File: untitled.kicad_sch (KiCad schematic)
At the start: 10 parts, among them IC1 MSPM0C1103SDGS20R, J1 Conn_01x10_Socket, SW1 SW_MEC_5G, SW2 SW_MEC_5G, U1 FZ2812-5050

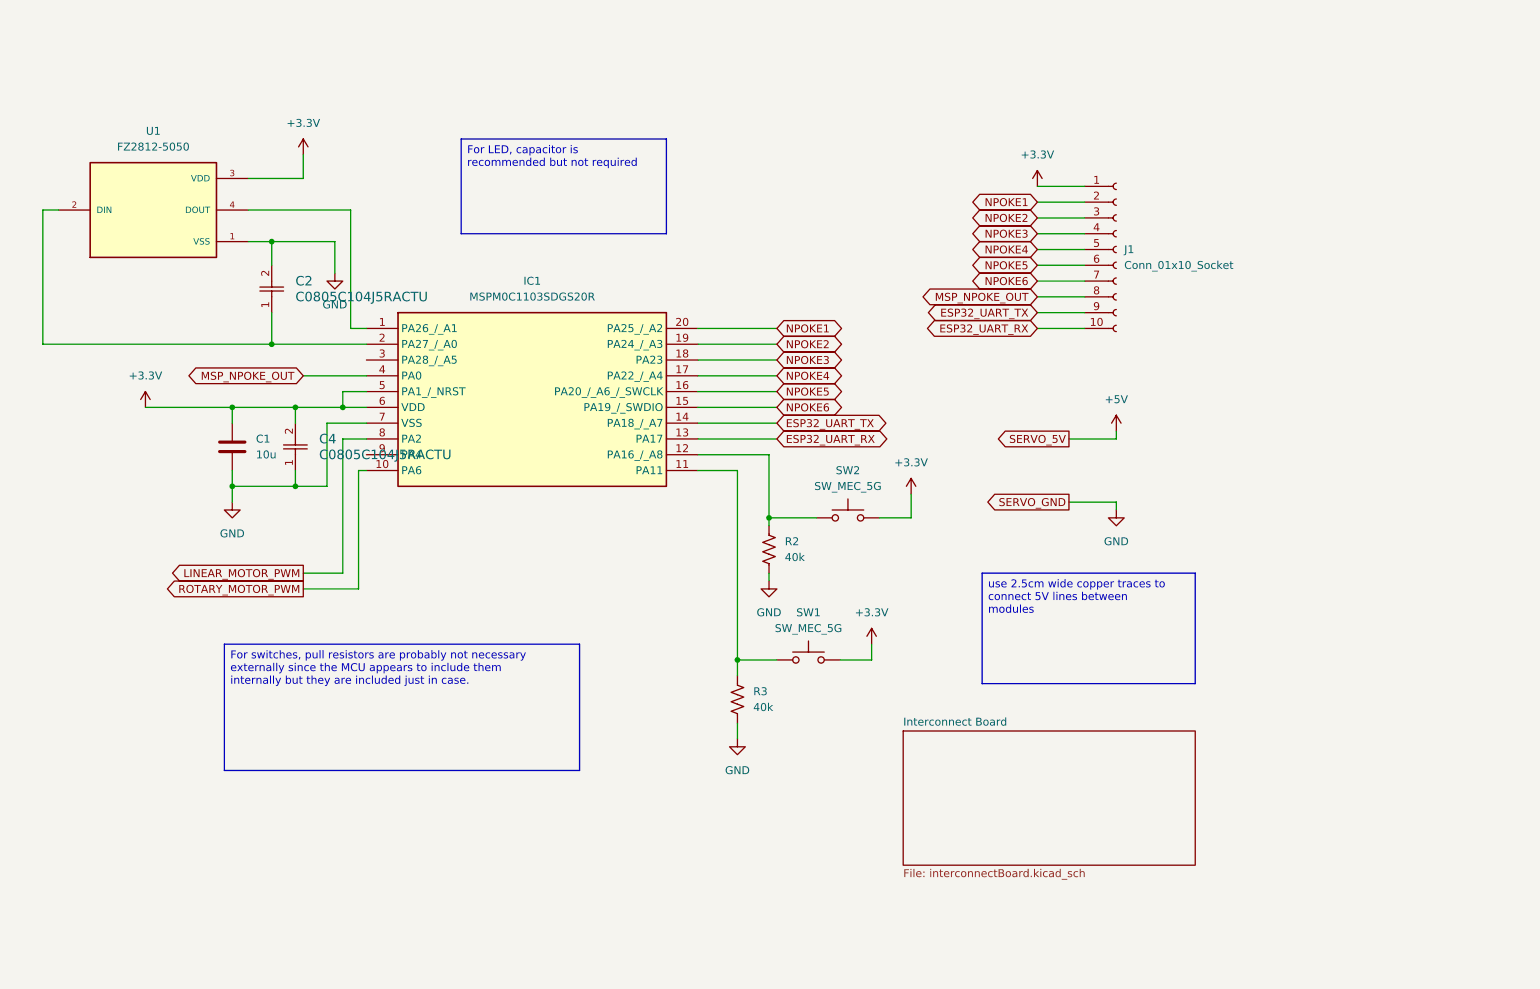
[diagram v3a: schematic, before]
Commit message: schem Rev 1 Ready for layout
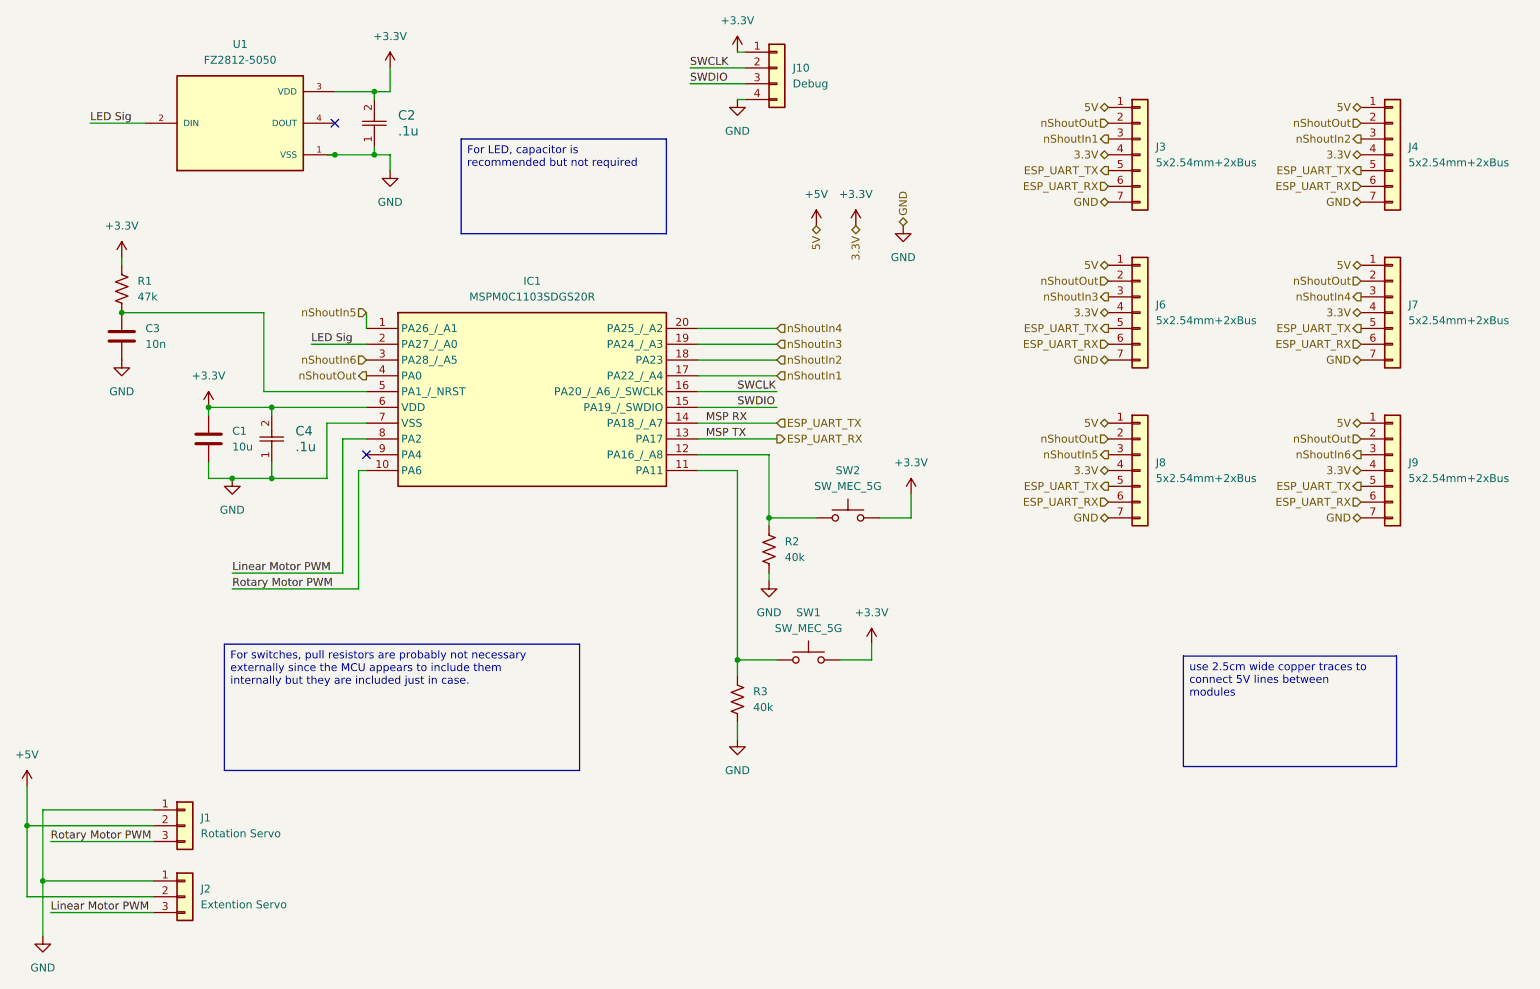
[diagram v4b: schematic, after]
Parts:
- removed J1: Conn_01x10_Socket, symbol Connector:Conn_01x10_Socket
- added C3: 10n, symbol Device:C
- added J1: Rotation Servo, symbol Connector_Generic:Conn_01x03
- added J10: Debug, symbol Connector_Generic:Conn_01x04
- added J2: Extention Servo, symbol Connector_Generic:Conn_01x03
- added J3, J4, J6, J7, J8, J9: 5x2.54mm+2xBus, symbol Connector_Generic:Conn_01x07
- added R1: 47k, symbol Device:R_US
- C2, C4: value C0805C104J5RACTU -> .1u
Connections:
- net +3.3V: now also C2.2, J10.1 (Pin_1), J3.4 (Pin_4), J4.4 (Pin_4), J6.4 (Pin_4), J7.4 (Pin_4), J8.4 (Pin_4), J9.4 (Pin_4), R1.1; no longer IC1.5 (PA1_/_NRST)
- net +5V: now also J1.2 (Pin_2), J2.2 (Pin_2), J3.1 (Pin_1), J4.1 (Pin_1), J6.1 (Pin_1), J7.1 (Pin_1), J8.1 (Pin_1), J9.1 (Pin_1)
- net GND: now also C2.1, C3.2, J1.1 (Pin_1), J10.4 (Pin_4), J2.1 (Pin_1), J3.7 (Pin_7), J4.7 (Pin_7), J6.7 (Pin_7), J7.7 (Pin_7), J8.7 (Pin_7), J9.7 (Pin_7); no longer C2.2
- net LED Sig: now reaches IC1.2 (PA27_/_A0), U1.2 (DIN)
- net LED Sig: no longer C2.1
- net at U1.4 (DOUT): no longer IC1.1 (PA26_/_A1)
- net nShoutIn6: now reaches IC1.3 (PA28_/_A5)
- net nShoutIn6: now also J9.3 (Pin_3)
- net ESP32_UART_RX renamed ESP_UART_RX
- net ESP_UART_RX: now also J3.6 (Pin_6), J4.6 (Pin_6), J6.6 (Pin_6), J7.6 (Pin_6), J8.6 (Pin_6), J9.6 (Pin_6)
- net ESP32_UART_TX renamed ESP_UART_TX
- net ESP_UART_TX: now also J3.5 (Pin_5), J4.5 (Pin_5), J6.5 (Pin_5), J7.5 (Pin_5), J8.5 (Pin_5), J9.5 (Pin_5)
- net LINEAR_MOTOR_PWM renamed Linear Motor PWM
- net Linear Motor PWM: now also J2.3 (Pin_3)
- net MSP_NPOKE_OUT renamed nShoutOut
- net nShoutOut: now also J3.2 (Pin_2), J4.2 (Pin_2), J6.2 (Pin_2), J7.2 (Pin_2), J8.2 (Pin_2), J9.2 (Pin_2)
- net NPOKE1 renamed nShoutIn4
- net nShoutIn4: now also J7.3 (Pin_3)
- net NPOKE2 renamed nShoutIn3
- net nShoutIn3: now also J6.3 (Pin_3)
- net NPOKE3 renamed nShoutIn2
- net nShoutIn2: now also J4.3 (Pin_3)
- net NPOKE4 renamed nShoutIn1
- net nShoutIn1: now also J3.3 (Pin_3)
- net NPOKE5 renamed SWCLK
- net SWCLK: now also J10.2 (Pin_2)
- net NPOKE6 renamed SWDIO
- net SWDIO: now also J10.3 (Pin_3)
- net ROTARY_MOTOR_PWM renamed Rotary Motor PWM
- net Rotary Motor PWM: now also J1.3 (Pin_3)
- new net: C3.1, IC1.5 (PA1_/_NRST), R1.2
- new net nShoutIn5: IC1.1 (PA26_/_A1), J8.3 (Pin_3)
- no-connect marks 0 -> 2
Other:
- removed sheet Interconnect Board
- company: (none) -> WPI
- title: (none) -> Module Board
- moved on the sheet: C1, C4, U1

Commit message: Refrences Changed, Root file fixed, UART Note Added
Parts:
- renumbered C2 to C1, C3 to C2, C1 to C3, J10 to J1, J3 to J2, J4 to J3, J6 to J4, J7 to J5, J8 to J6, J9 to J7, J1 to J8, J2 to J9, SW2 to SW1, SW1 to SW2

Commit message: Direcctory reorganization footprints added
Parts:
- C?: renamed from C2; footprint (none) -> Capacitor_SMD:C_0805_2012Metric_Pad1.18x1.45mm_HandSolder
- C?: renamed from C4; footprint CAPC220145_88N_KEM -> Capacitor_SMD:C_0805_2012Metric_Pad1.18x1.45mm_HandSolder
- C?: renamed from C3; footprint (none) -> Capacitor_SMD:C_0805_2012Metric_Pad1.18x1.45mm_HandSolder
- C?: renamed from C1; footprint CAPC220145_88N_KEM -> Capacitor_SMD:C_0805_2012Metric_Pad1.18x1.45mm_HandSolder
- IC?: renamed from IC1; footprint SOP50P490X110-20N -> Rose Actuator Library:MSPM0C1103SDGS20R
- J?: renamed from J2; footprint (none) -> Rose Actuator Library:InterModuleConnectorMside
- J?: renamed from J4; footprint (none) -> Rose Actuator Library:InterModuleConnectorMside
- J?: renamed from J6; footprint (none) -> Rose Actuator Library:InterModuleConnectorMside
- J?: renamed from J3; footprint (none) -> Rose Actuator Library:InterModuleConnectorMside
- J?: renamed from J8; footprint (none) -> Connector_PinHeader_2.54mm:PinHeader_1x03_P2.54mm_Vertical
- J?: renamed from J7; footprint (none) -> Rose Actuator Library:InterModuleConnectorMside
- J?: renamed from J1; footprint (none) -> Connector_PinSocket_2.54mm:PinSocket_1x04_P2.54mm_Vertical
- J?: renamed from J5; footprint (none) -> Rose Actuator Library:InterModuleConnectorMside
- J?: renamed from J9; footprint (none) -> Connector_PinHeader_2.54mm:PinHeader_1x03_P2.54mm_Vertical
- R?: renamed from R1; footprint (none) -> Resistor_SMD:R_1206_3216Metric_Pad1.30x1.75mm_HandSolder
- R?: renamed from R3; footprint (none) -> Resistor_SMD:R_1206_3216Metric_Pad1.30x1.75mm_HandSolder
- R?: renamed from R2; footprint (none) -> Resistor_SMD:R_1206_3216Metric_Pad1.30x1.75mm_HandSolder
- U?: renamed from U1; footprint FZ2812-5050:LED_FZ2812-5050 -> Rose Actuator Library:LED_FZ2812-5050
- renumbered SW2 to SW?, SW1 to SW?

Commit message: Improved amplifier
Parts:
- gave numbers to parts that had none: 20
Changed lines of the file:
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@@
 		(dnp no)
 		(fields_autoplaced yes)
-		(property "Reference" "#PWR?"
+		(property "Reference" "#PWR011"
 			(at 48.26 97.79 0)
 			(effects
@@
 		(dnp no)
 		(fields_autoplaced yes)
-		(property "Reference" "#PWR?"
+		(property "Reference" "#PWR016"
 			(at 15.24 144.78 0)
 			(effects
@@
 		(dnp no)
 		(fields_autoplaced yes)
-		(property "Reference" "#PWR?"
+		(property "Reference" "#PWR015"
 			(at 129.54 139.7 0)
 			(effects
@@
 		(dnp no)
 		(fields_autoplaced yes)
-		(property "Reference" "J?"
+		(property "Reference" "J2"
 			(at 196.85 38.0999 0)
 			(effects
@@
 		(dnp no)
 		(fields_autoplaced yes)
-		(property "Reference" "#PWR?"
+		(property "Reference" "#PWR013"
 			(at 134.62 114.3 0)
 			(effects
@@
 		(dnp no)
 		(fields_autoplaced yes)
-		(property "Reference" "J?"
+		(property "Reference" "J4"
 			(at 196.85 63.4999 0)
 			(effects
@@
 		(dnp no)
 		(fields_autoplaced yes)
-		(property "Reference" "#PWR?"
+		(property "Reference" "#PWR02"
 			(at 73.66 29.21 0)
 			(effects
@@
 		(dnp no)
 		(fields_autoplaced yes)
-		(property "Reference" "J?"
+		(property "Reference" "J6"
 			(at 196.85 88.8999 0)
 			(effects
@@
 		(dnp no)
 		(fields_autoplaced yes)
-		(property "Reference" "R?"
+		(property "Reference" "R1"
 			(at 33.02 59.6899 0)
 			(effects
@@
 		(dnp no)
 		(fields_autoplaced yes)
-		(property "Reference" "C?"
+		(property "Reference" "C2"
 			(at 34.29 67.3099 0)
 			(effects
@@
 		(dnp no)
 		(fields_autoplaced yes)
-		(property "Reference" "J?"
+		(property "Reference" "J3"
 			(at 237.49 38.0999 0)
 			(effects
@@
 		(dnp no)
 		(fields_autoplaced yes)
-		(property "Reference" "#PWR?"
+		(property "Reference" "#PWR01"
 			(at 129.54 26.67 0)
 			(effects
@@
 		(dnp no)
 		(fields_autoplaced yes)
-		(property "Reference" "#PWR?"
+		(property "Reference" "#PWR08"
 			(at 30.48 59.69 0)
 			(effects
@@
 		(dnp no)
 		(fields_autoplaced yes)
-		(property "Reference" "R?"
+		(property "Reference" "R3"
 			(at 132.08 125.7299 0)
 			(effects
@@
 		(dnp no)
 		(fields_autoplaced yes)
-		(property "Reference" "U?"
+		(property "Reference" "U1"
 			(at 49.53 21.59 0)
 			(effects
@@
 		(dnp no)
 		(fields_autoplaced yes)
-		(property "Reference" "SW?"
+		(property "Reference" "SW2"
 			(at 140.97 113.03 0)
 			(effects
@@
 		(dnp no)
 		(fields_autoplaced yes)
-		(property "Reference" "#PWR?"
+		(property "Reference" "#PWR05"
 			(at 142.24 54.61 0)
 			(effects
@@
 		(dnp no)
 		(fields_autoplaced yes)
-		(property "Reference" "#PWR?"
+		(property "Reference" "#PWR014"
 			(at 151.13 121.92 0)
 			(effects
@@
 		(dnp no)
 		(fields_autoplaced yes)
-		(property "Reference" "C?"
+		(property "Reference" "C4"
 			(at 58.42 83.8199 90)
 			(effects
@@
 		(dnp no)
 		(fields_autoplaced yes)
-		(property "Reference" "#PWR?"
+		(property "Reference" "#PWR012"
 			(at 157.48 97.79 0)
 			(effects
@@
 		(dnp no)
 		(fields_autoplaced yes)
-		(property "Reference" "R?"
+		(property "Reference" "R2"
 			(at 137.16 101.5999 0)
 			(effects
@@
 		(dnp no)
 		(fields_autoplaced yes)
-		(property "Reference" "#PWR?"
+		(property "Reference" "#PWR017"
 			(at 17.78 171.45 0)
 			(effects
@@
 		(dnp no)
 		(fields_autoplaced yes)
-		(property "Reference" "#PWR?"
+		(property "Reference" "#PWR010"
 			(at 44.45 83.82 0)
 			(effects
@@
 		(dnp no)
 		(fields_autoplaced yes)
-		(property "Reference" "J?"
+		(property "Reference" "J8"
 			(at 43.18 146.0499 0)
 			(effects
@@
 		(dnp no)
 		(fields_autoplaced yes)
-		(property "Reference" "J?"
+		(property "Reference" "J7"
 			(at 237.49 88.8999 0)
 			(effects
@@
 		(dnp no)
 		(fields_autoplaced yes)
-		(property "Reference" "#PWR?"
+		(property "Reference" "#PWR07"
 			(at 156.21 57.15 0)
 			(effects
@@
 		(dnp no)
 		(fields_autoplaced yes)
-		(property "Reference" "IC?"
+		(property "Reference" "IC1"
 			(at 96.52 59.69 0)
 			(effects
@@
 		(dnp no)
 		(fields_autoplaced yes)
-		(property "Reference" "C?"
+		(property "Reference" "C3"
 			(at 48.26 83.8199 0)
 			(effects
@@
 		(dnp no)
 		(fields_autoplaced yes)
-		(property "Reference" "#PWR?"
+		(property "Reference" "#PWR09"
 			(at 30.48 78.74 0)
 			(effects
@@
 		(dnp no)
 		(fields_autoplaced yes)
-		(property "Reference" "#PWR?"
+		(property "Reference" "#PWR04"
 			(at 73.66 48.26 0)
 			(effects
@@
 		(dnp no)
 		(fields_autoplaced yes)
-		(property "Reference" "J?"
+		(property "Reference" "J1"
 			(at 138.43 25.3999 0)
 			(effects
@@
 		(dnp no)
 		(fields_autoplaced yes)
-		(property "Reference" "J?"
+		(property "Reference" "J5"
 			(at 237.49 63.4999 0)
 			(effects
@@
 		(dnp no)
 		(fields_autoplaced yes)
-		(property "Reference" "SW?"
+		(property "Reference" "SW1"
 			(at 147.32 90.17 0)
 			(effects
@@
 		(dnp no)
 		(fields_autoplaced yes)
-		(property "Reference" "C?"
+		(property "Reference" "C1"
 			(at 74.93 33.0199 90)
 			(effects
@@
 		(dnp no)
 		(fields_autoplaced yes)
-		(property "Reference" "#PWR?"
+		(property "Reference" "#PWR03"
 			(at 129.54 36.83 0)
 			(effects
@@
 		(dnp no)
 		(fields_autoplaced yes)
-		(property "Reference" "J?"
+		(property "Reference" "J9"
 			(at 43.18 157.4799 0)
 			(effects
@@
 		(dnp no)
 		(fields_autoplaced yes)
-		(property "Reference" "#PWR?"
+		(property "Reference" "#PWR06"
 			(at 148.59 54.61 0)
 			(effects
